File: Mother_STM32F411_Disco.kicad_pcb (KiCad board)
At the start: 2 copper layers, 29 parts, among them U1 ESP32-DEVKIT-V1

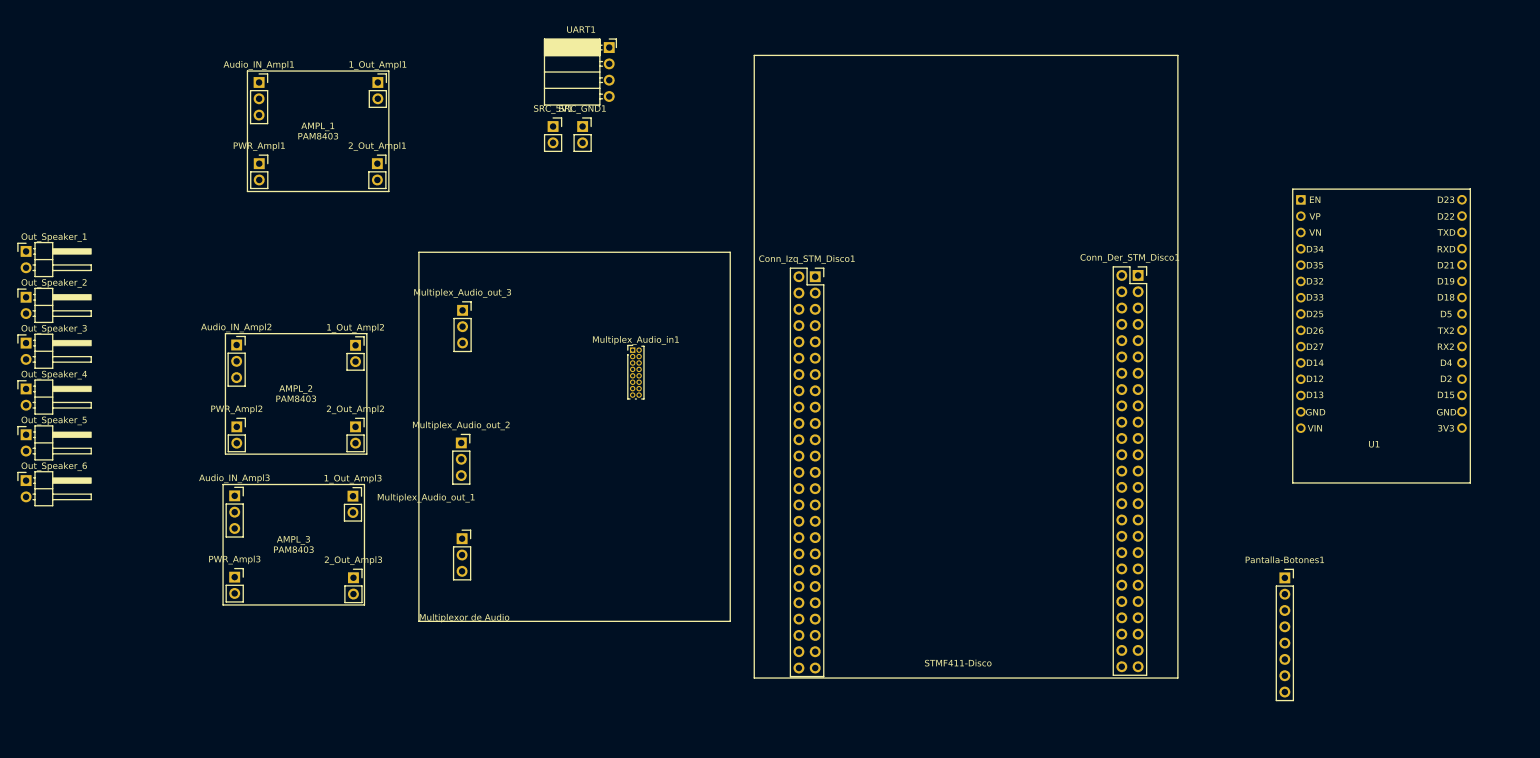
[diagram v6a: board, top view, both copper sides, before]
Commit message: Huellas agregadas, src_pwr agregado
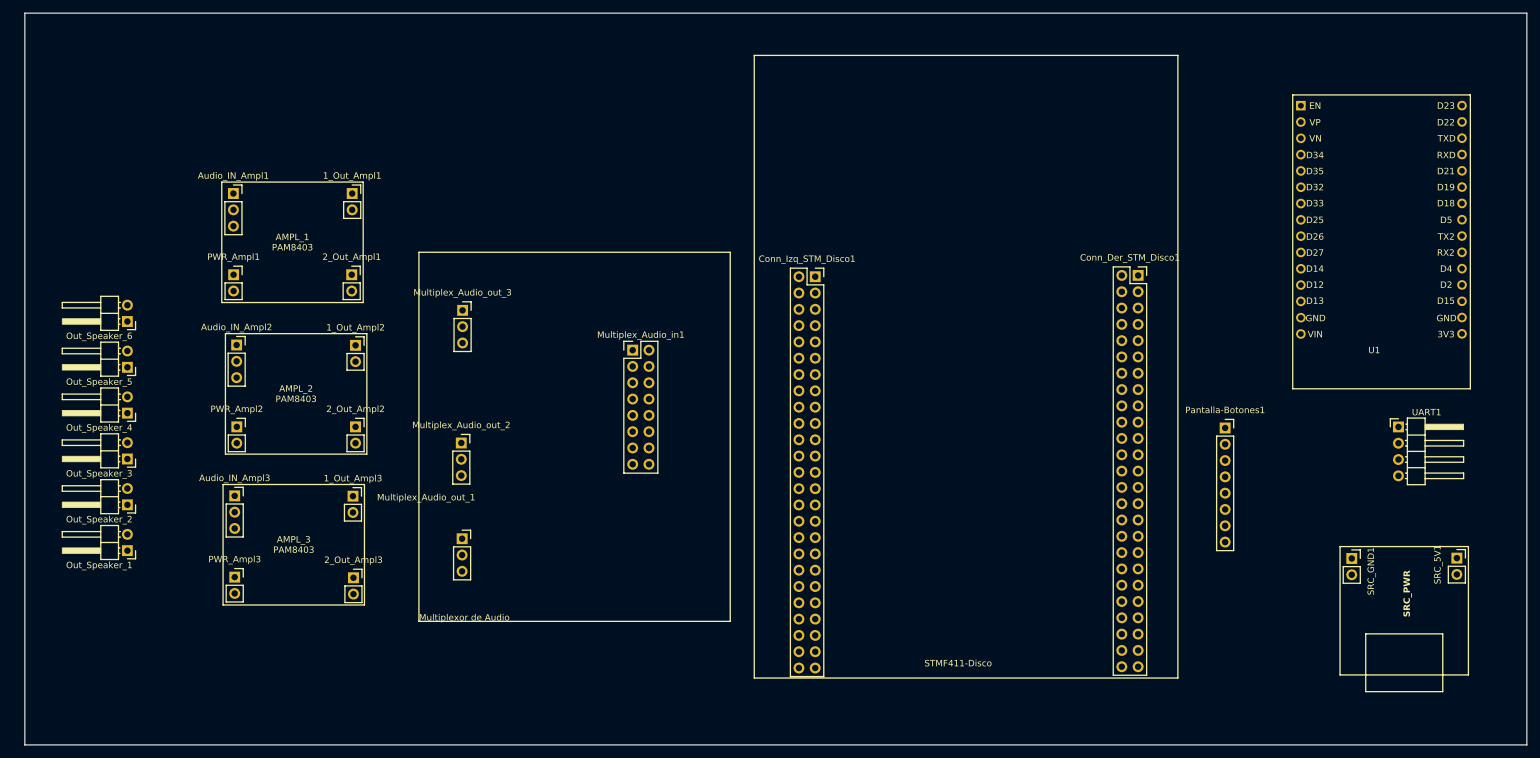
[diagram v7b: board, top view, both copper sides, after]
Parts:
- Multiplex_Audio_in1: footprint Connector_PinHeader_1.00mm:PinHeader_2x08_P1.00mm_Vertical -> Connector_PinHeader_2.54mm:PinHeader_2x08_P2.54mm_Vertical
- UART1: footprint Connector_PinSocket_2.54mm:PinSocket_1x04_P2.54mm_Horizontal -> Connector_PinHeader_2.54mm:PinHeader_1x04_P2.54mm_Horizontal
- moved SRC_5V1 156.0 mm to (247.1, 120.9)
- moved SRC_GND1 137.4 mm to (230.7, 121.0)
- moved UART1 136.4 mm to (238.0, 100.5)
- moved Out_Speaker_1 49.2 mm to (40.0, 119.7), turned to 180 degrees
- moved Out_Speaker_2 36.0 mm to (40.0, 112.6), turned to 180 degrees
- moved Out_Speaker_6 29.4 mm to (40.0, 84.0), turned to 180 degrees
- moved Pantalla-Botones1 25.1 mm to (211.0, 100.6)
- moved Out_Speaker_3 24.0 mm to (40.0, 105.5), turned to 180 degrees
- moved Out_Speaker_5 19.0 mm to (40.0, 91.2), turned to 180 degrees
- moved 1_Out_Ampl1 17.8 mm to (75.0, 64.1)
- moved 2_Out_Ampl1 17.8 mm to (74.9, 76.8)
- moved Audio_IN_Ampl1 17.8 mm to (56.5, 64.1)
- moved PWR_Ampl1 17.8 mm to (56.5, 76.8)
- moved Out_Speaker_4 16.2 mm to (40.0, 98.3), turned to 180 degrees
- moved U1 14.7 mm to (222.8, 50.4)
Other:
- board outline added: 234 x 114 mm
- board text added: "SRC_PWR"

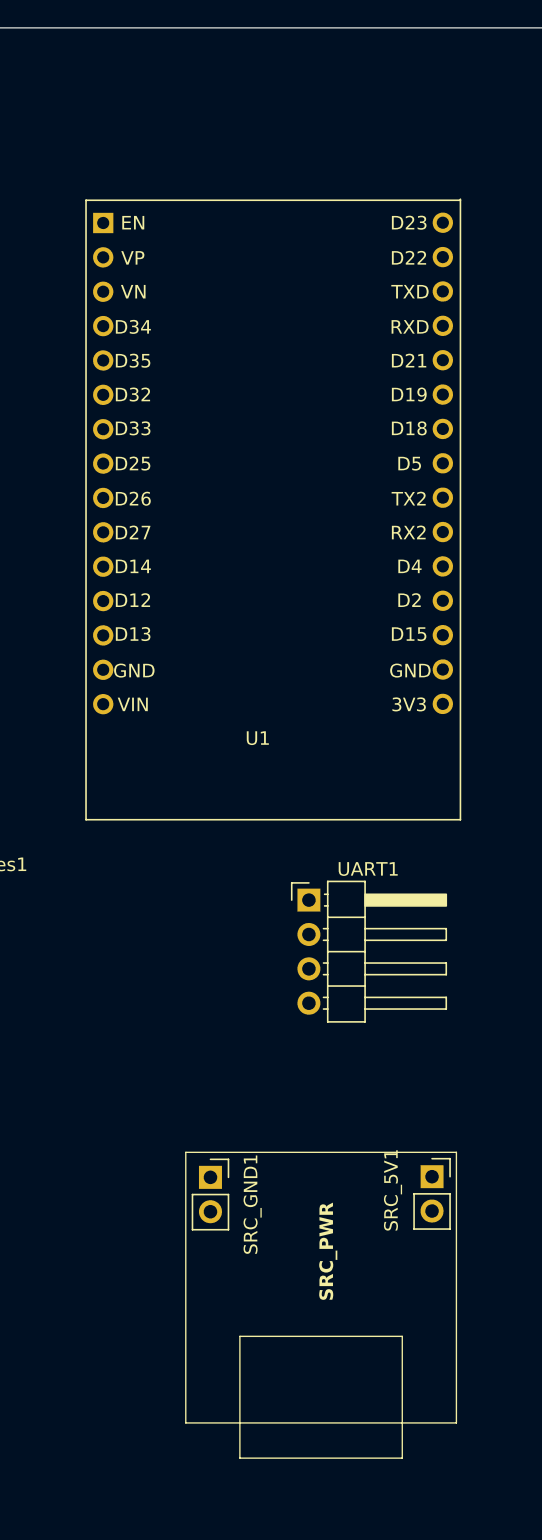
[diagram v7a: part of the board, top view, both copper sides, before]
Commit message: SA'18: agregue pistas de la ESP32 y actualice el footprint
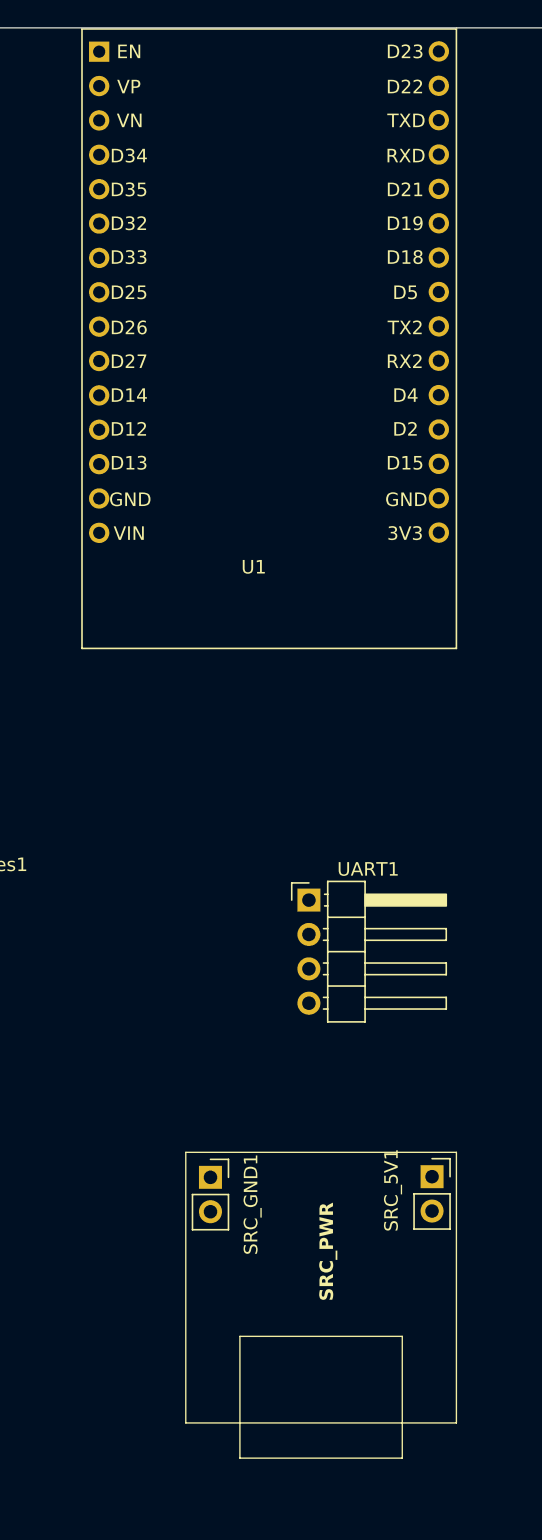
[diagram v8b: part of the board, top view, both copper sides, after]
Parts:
- moved U1 12.7 mm to (222.5, 37.8)
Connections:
- U1 pad 14: unconnected-(U1-D22-Pad14) -> /GND
- U1 pad 15: unconnected-(U1-D23-Pad15) -> /5V
- U1 pad 17: unconnected-(U1-VP-Pad17) -> /GND
- U1 pad 2: Net-(U1-GND-Pad2) -> unconnected-(U1-VP-Pad2)
- U1 pad 21: unconnected-(U1-D32-Pad21) -> /PA15
- U1 pad 22: unconnected-(U1-D33-Pad22) -> /PB3
- U1 pad 29: Net-(U1-GND-Pad2) -> unconnected-(U1-D22-Pad29)
